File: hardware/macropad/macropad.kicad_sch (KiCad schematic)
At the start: 33 parts, among them J1 SWD, J2 USB_C_Receptacle, J4 display(4x1), J6 Enc2, J7 Enc1, SW1 SW_Push, SW11 SW_Push, SW2 SW_Push, SW3 SW_Push, SW4 SW_Push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

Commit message: added usb-c receptacle footprint
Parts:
- J2: footprint (none) -> usbc:TYPE-C-SMD_U263-163N-4GS1735
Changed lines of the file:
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@@
 			)
 		)
-		(property "Footprint" ""
+		(property "Footprint" "usbc:TYPE-C-SMD_U263-163N-4GS1735"
 			(at 361.95 170.18 0)
 			(effects

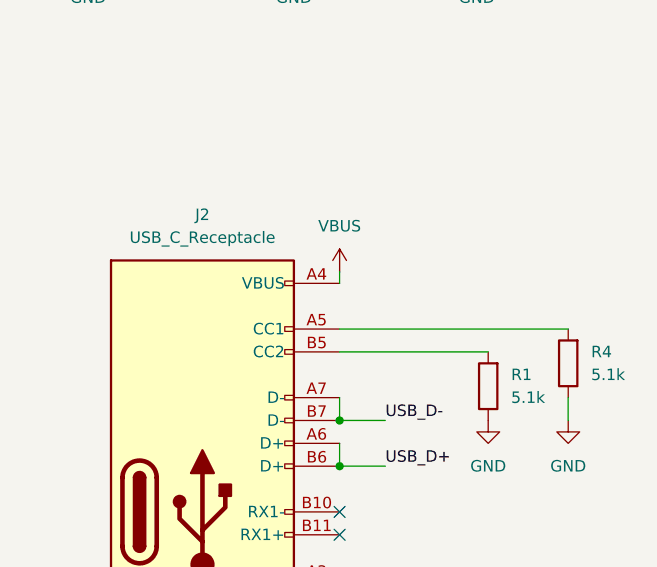
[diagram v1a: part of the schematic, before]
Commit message: erc for macropad checked
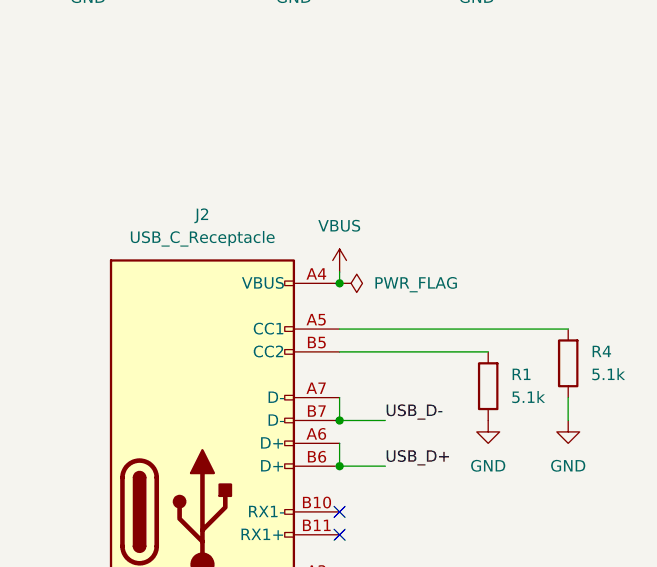
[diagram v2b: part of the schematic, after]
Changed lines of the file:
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@@
 	)
 	(junction
+		(at 373.38 144.78)
+		(diameter 0)
+		(color 0 0 0 0)
+	)
+	(junction
 		(at 288.29 53.34)
 		(diameter 0)
@@
 					(unit 1)
 				)
+			)
+		)
+	)
+	(symbol
+		(lib_id "power:PWR_FLAG")
+		(at 373.38 144.78 270)
+		(unit 1)
+		(exclude_from_sim no)
+		(in_bom yes)
+		(on_board yes)
+		(dnp no)
+		(fields_autoplaced yes)
+		(property "Reference" "#FLG01"
+			(at 375.285 144.78 0)
+			(effects
+				(font
+					(size 1.27 1.27)
+				)
+				(hide yes)
+			)
+		)
+		(property "Value" "PWR_FLAG"
+			(at 377.19 144.7799 90)
+			(effects
+				(font
+					(size 1.27 1.27)
+				)
+				(justify left)
+			)
+		)
+		(property "Footprint" ""
+			(at 373.38 144.78 0)
+			(effects
+				(font
+					(size 1.27 1.27)
+				)
+				(hide yes)
+			)
+		)
+		(property "Datasheet" "~"
+			(at 373.38 144.78 0)
+			(effects
+				(font
+					(size 1.27 1.27)
+				)
+				(hide yes)
+			)
+		)
+		(property "Description" "Special symbol for telling ERC where power comes from"
+			(at 373.38 144.78 0)
+			(effects
+				(font
+					(size 1.27 1.27)
+				)
+				(hide yes)
+			)
+		)
+		(pin "1"
+		)
+		(instances
+			(project ""
+				(path "/228dc472-b306-4e5f-8dc5-2bf23eb4978d"
+					(reference "#FLG01")
+					(unit 1)
+				)

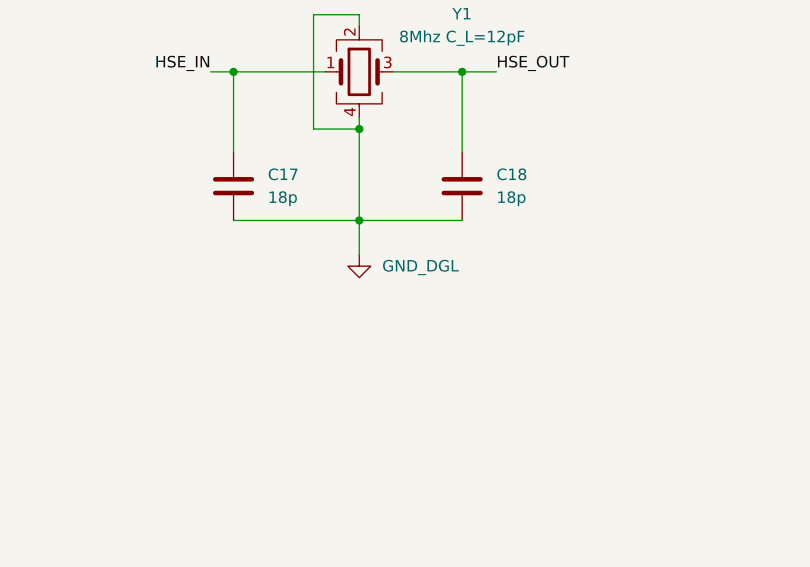
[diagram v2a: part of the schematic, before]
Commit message: added usba fp, updated pcb, 5v to vbus
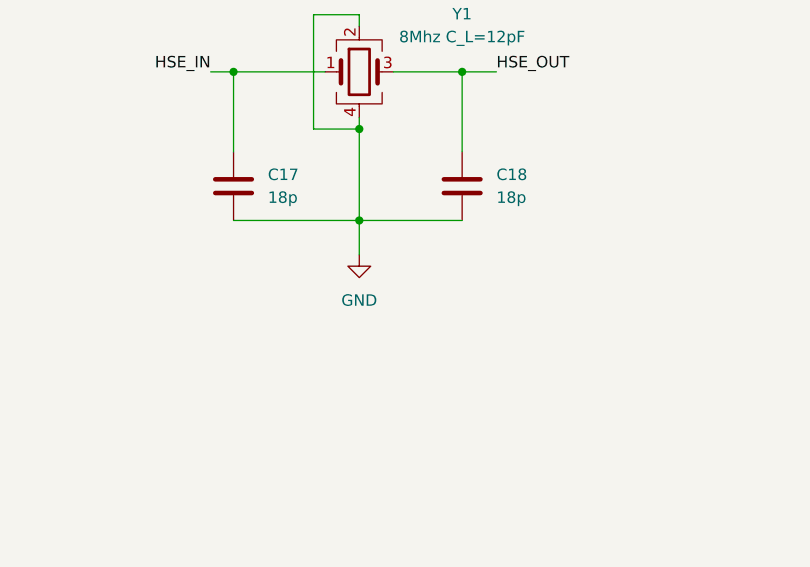
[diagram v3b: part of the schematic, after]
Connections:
- net GND_DGL is gone; now on net GND: C17.2, C18.2, Y1.2, Y1.4
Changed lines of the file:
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@@
 			)
 		)
-		(property "Value" "GND_DGL"
-			(at 104.14 147.3199 0)
+		(property "Value" "GND"
+			(at 101.6 151.13 0)
 			(effects
 				(font
 					(size 1.27 1.27)
 				)
-				(justify left)
 			)
 		)

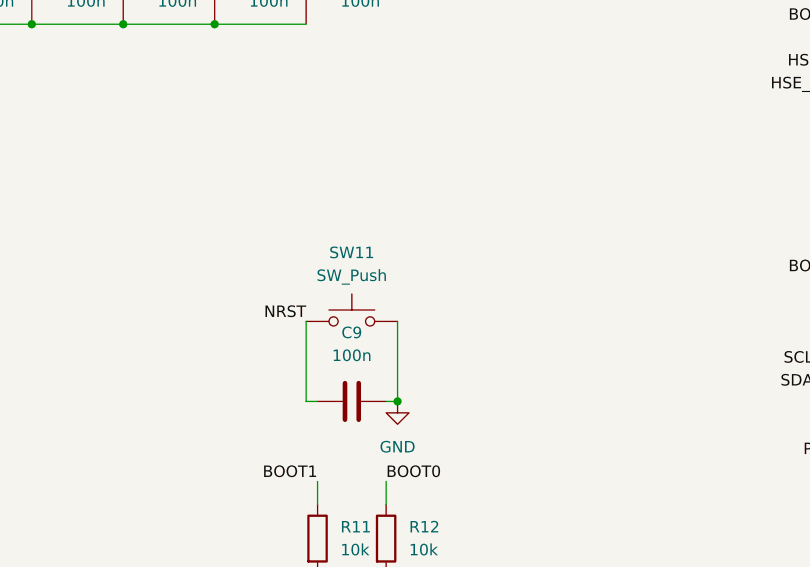
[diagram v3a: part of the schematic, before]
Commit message: replaced buttons with pads
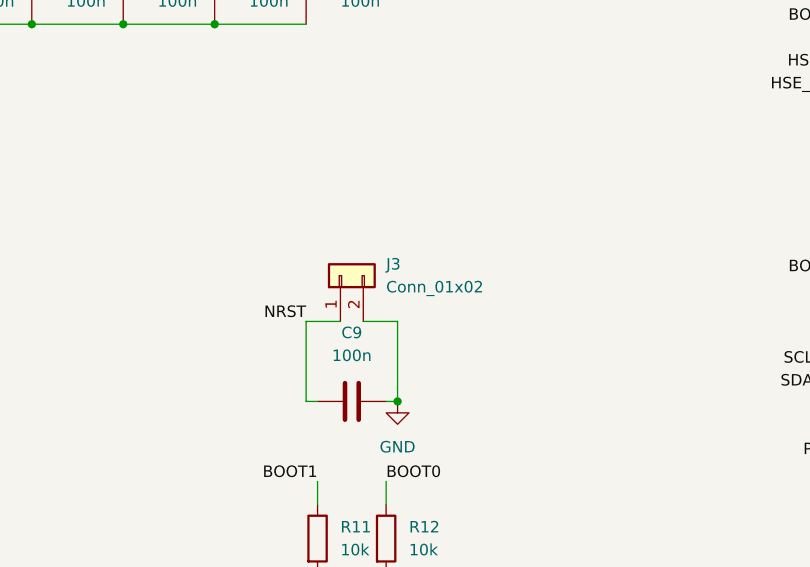
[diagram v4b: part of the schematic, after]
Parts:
- removed SW11: SW_Push, Button_Switch_SMD:SW_Push_1P1T_NO_E-Switch_TL3301NxxxxxG, symbol Switch:SW_Push
- added J3: Conn_01x02, Connector_Wire:SolderWire-0.5sqmm_1x02_P4.6mm_D0.9mm_OD2.1mm, symbol Connector_Generic:Conn_01x02
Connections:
- net GND: now also J3.2 (Pin_2)
- net NRST: now also J3.1 (Pin_1)
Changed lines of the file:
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@@
 	(wire
 		(pts
+			(xy 118.11 80.01) (xy 121.92 80.01)
+		)
+		(stroke
+			(width 0)
+			(type default)
+		)
+	)
+	(wire
+		(pts
 			(xy 96.52 119.38) (xy 96.52 132.08)
 		)
@@
 	(wire
 		(pts
+			(xy 111.76 80.01) (xy 115.57 80.01)
+		)
+		(stroke
+			(width 0)
+			(type default)
+		)
+	)
+	(wire
+		(pts
 			(xy 377.19 49.53) (xy 378.46 49.53)
 		)
@@
 	)
 	(symbol
-		(lib_id "Switch:SW_Push")
-		(at 116.84 80.01 0)
-		(unit 1)
-		(exclude_from_sim no)
-		(in_bom yes)
-		(on_board yes)
-		(dnp no)
-		(fields_autoplaced yes)
-		(property "Reference" "SW11"
-			(at 116.84 72.39 0)
-			(effects
-				(font
-					(size 1.27 1.27)
-				)
-			)
-		)
-		(property "Value" "SW_Push"
-			(at 116.84 74.93 0)
-			(effects
-				(font
-					(size 1.27 1.27)
-				)
-			)
-		)
-		(property "Footprint" "Button_Switch_SMD:SW_Push_1P1T_NO_E-Switch_TL3301NxxxxxG"
-			(at 116.84 74.93 0)
-			(effects
-				(font
-					(size 1.27 1.27)
-				)
-				(hide yes)
-			)
-		)
-		(property "Datasheet" "~"
-			(at 116.84 74.93 0)
-			(effects
-				(font
-					(size 1.27 1.27)
-				)
-				(hide yes)
-			)
-		)
-		(property "Description" "Push button switch, generic, two pins"
-			(at 116.84 80.01 0)
-			(effects
-				(font
-					(size 1.27 1.27)
-				)
-				(hide yes)
-			)
-		)
-		(pin "2"
-		)
-		(pin "1"
-		)
-		(instances
-			(project ""
-				(path "/228dc472-b306-4e5f-8dc5-2bf23eb4978d"
-					(reference "SW11")
-					(unit 1)
-				)
-			)
-		)
-	)
-	(symbol
 		(lib_id "power:GND")
 		(at 389.89 160.02 0)
@@
 					(unit 1)
 				)
+			)
+		)
+	)
+	(symbol
+		(lib_id "Connector_Generic:Conn_01x02")
+		(at 115.57 74.93 90)
+		(unit 1)
+		(exclude_from_sim no)
+		(in_bom yes)
+		(on_board yes)
+		(dnp no)
+		(fields_autoplaced yes)
+		(property "Reference" "J3"
+			(at 120.65 73.6599 90)
+			(effects
+				(font
+					(size 1.27 1.27)
+				)
+				(justify right)
+			)
+		)
+		(property "Value" "Conn_01x02"
+			(at 120.65 76.1999 90)
+			(effects
+				(font
+					(size 1.27 1.27)
+				)
+				(justify right)
+			)
+		)
+		(property "Footprint" "Connector_Wire:SolderWire-0.5sqmm_1x02_P4.6mm_D0.9mm_OD2.1mm"
+			(at 115.57 74.93 0)
+			(effects
+				(font
+					(size 1.27 1.27)
+				)
+				(hide yes)
+			)
+		)
+		(property "Datasheet" "~"
+			(at 115.57 74.93 0)
+			(effects
+				(font
+					(size 1.27 1.27)
+				)
+				(hide yes)
+			)
+		)
+		(property "Description" "Generic connector, single row, 01x02, script generated (kicad-library-utils/schlib/autogen/connector/)"
+			(at 115.57 74.93 0)
+			(effects
+				(font
+					(size 1.27 1.27)
+				)
+				(hide yes)
+			)
+		)
+		(pin "2"
+		)
+		(pin "1"
+		)
+		(instances
+			(project "macropad"
+				(path "/228dc472-b306-4e5f-8dc5-2bf23eb4978d"
+					(reference "J3")
+					(unit 1)
+				)

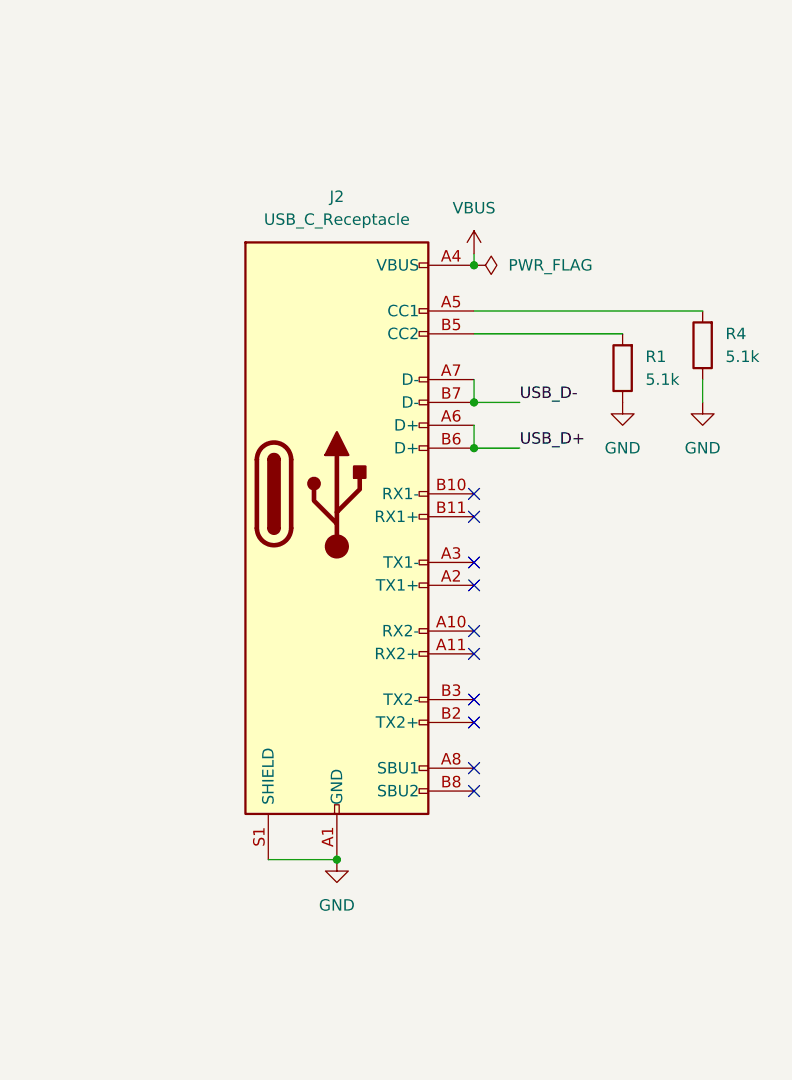
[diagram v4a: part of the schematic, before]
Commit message: updated usb-c receptacle footprint
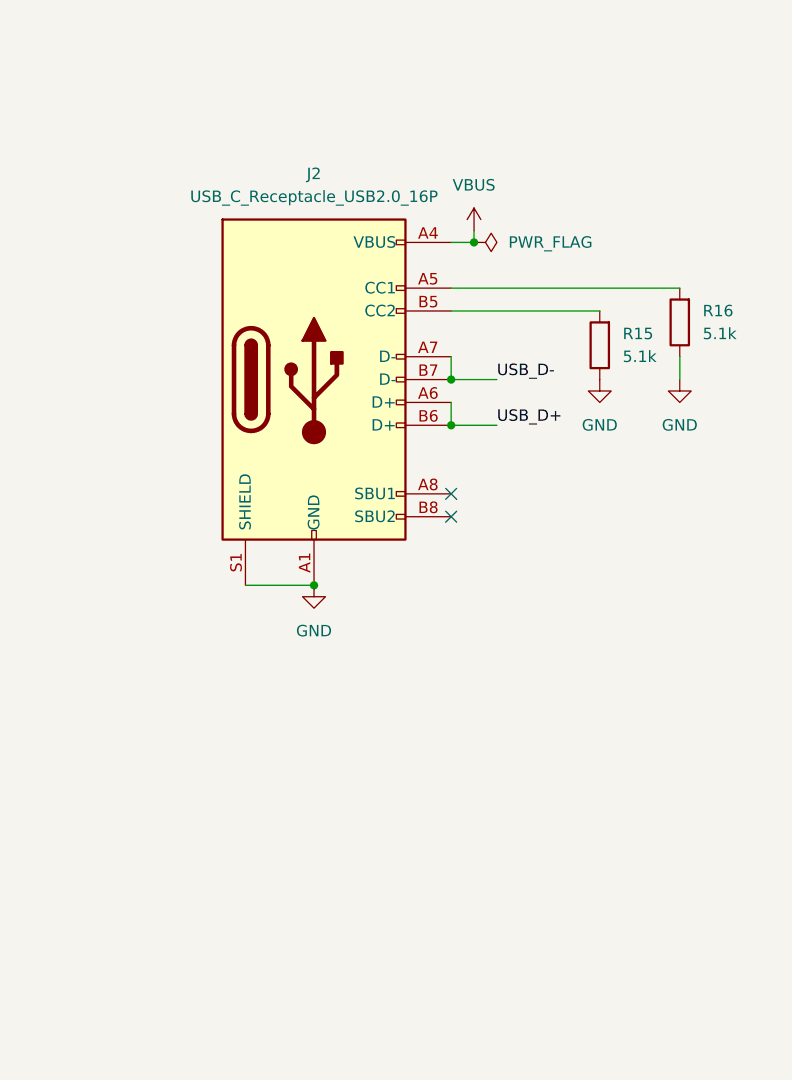
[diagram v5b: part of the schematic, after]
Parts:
- removed J2: USB_C_Receptacle, usbc:TYPE-C-SMD_U263-163N-4GS1735, symbol Connector:USB_C_Receptacle
- removed R1, R4: 5.1k, Resistor_SMD:R_0603_1608Metric, symbol Device:R
- added J2: USB_C_Receptacle_USB2.0_16P, usbc:TYPE-C-SMD_U263-163N-4GS1735, symbol Connector:USB_C_Receptacle_USB2.0_16P
- added R15, R16: 5.1k, Resistor_SMD:R_0603_1608Metric, symbol Device:R
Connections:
- net GND: now also J2.A1 (GND), J2.A12 (GND), J2.B1 (GND), J2.B12 (GND), J2.S1 (SHIELD), R15.1, R16.1
- net USB_D+: now also J2.A6 (D+), J2.B6 (D+)
- net USB_D-: now also J2.A7 (D-), J2.B7 (D-)
- net VBUS: now also J2.A4 (VBUS), J2.A9 (VBUS), J2.B4 (VBUS), J2.B9 (VBUS)
- new net: J2.A5 (CC1), R16.2
- new net: J2.B5 (CC2), R15.2
- no-connect marks 17 -> 9

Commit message: updated. comments in whatsapp
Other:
- moved on the sheet: C1, C17, C18, C2, C3, C4, C5, C6, C8, C9, J1, J3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

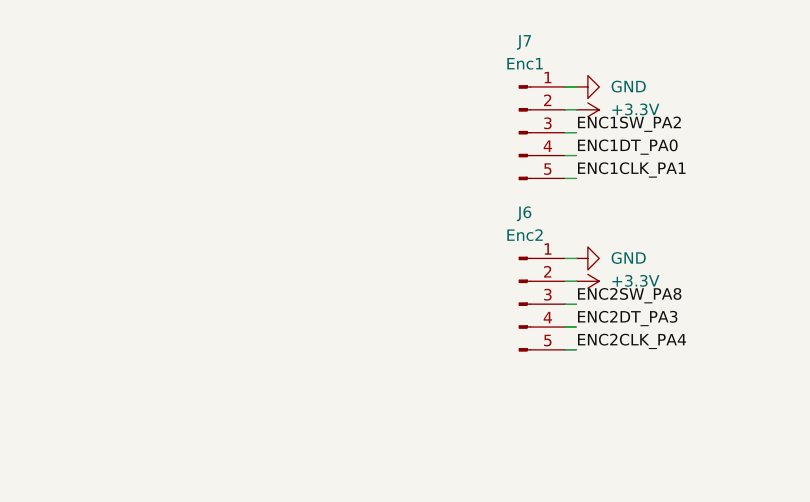
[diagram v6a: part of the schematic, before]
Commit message: pcb macropad done
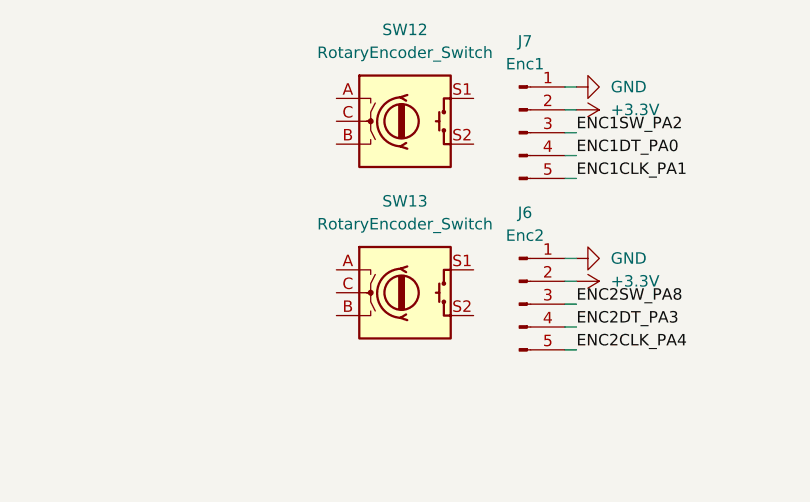
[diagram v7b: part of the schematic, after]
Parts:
- added SW12, SW13: RotaryEncoder_Switch, symbol Device:RotaryEncoder_Switch
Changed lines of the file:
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@@
+	)
+	(symbol
+		(lib_id "Device:RotaryEncoder_Switch")
+		(at 359.41 45.72 0)
+		(unit 1)
+		(exclude_from_sim no)
+		(in_bom yes)
+		(on_board yes)
+		(dnp no)
+		(fields_autoplaced yes)
+		(property "Reference" "SW13"
+			(at 359.41 35.56 0)
+			(effects
+				(font
+					(size 1.27 1.27)
+				)
+			)
+		)
+		(property "Value" "RotaryEncoder_Switch"
+			(at 359.41 38.1 0)
+			(effects
+				(font
+					(size 1.27 1.27)
+				)
+			)
+		)
+		(property "Footprint" ""
+			(at 355.6 41.656 0)
+			(effects
+				(font
+					(size 1.27 1.27)
+				)
+				(hide yes)
+			)
+		)
+		(property "Datasheet" "~"
+			(at 359.41 39.116 0)
+			(effects
+				(font
+					(size 1.27 1.27)
+				)
+				(hide yes)
+			)
+		)
+		(property "Description" "Rotary encoder, dual channel, incremental quadrate outputs, with switch"
+			(at 359.41 45.72 0)
+			(effects
+				(font
+					(size 1.27 1.27)
+				)
+				(hide yes)
+			)
+		)
+		(pin "B"
+		)
+		(pin "S1"
+		)
+		(pin "C"
+		)
+		(pin "S2"
+		)
+		(pin "A"
+		)
+		(instances
+			(project "macropad"
+				(path "/228dc472-b306-4e5f-8dc5-2bf23eb4978d"
+					(reference "SW13")
+					(unit 1)
+				)
+			)
+		)
 	)
 	(symbol
@@
 					(unit 1)
 				)
+			)
+		)
+	)
+	(symbol
+		(lib_id "Device:RotaryEncoder_Switch")
+		(at 359.41 26.67 0)
+		(unit 1)
+		(exclude_from_sim no)
+		(in_bom yes)
+		(on_board yes)
+		(dnp no)
+		(fields_autoplaced yes)
+		(property "Reference" "SW12"
+			(at 359.41 16.51 0)
+			(effects
+				(font
+					(size 1.27 1.27)
+				)
+			)
+		)
+		(property "Value" "RotaryEncoder_Switch"
+			(at 359.41 19.05 0)
+			(effects
+				(font
+					(size 1.27 1.27)
+				)
+			)
+		)
+		(property "Footprint" ""
+			(at 355.6 22.606 0)
+			(effects
+				(font
+					(size 1.27 1.27)
+				)
+				(hide yes)
+			)
+		)
+		(property "Datasheet" "~"
+			(at 359.41 20.066 0)
+			(effects
+				(font
+					(size 1.27 1.27)
+				)
+				(hide yes)
+			)
+		)
+		(property "Description" "Rotary encoder, dual channel, incremental quadrate outputs, with switch"
+			(at 359.41 26.67 0)
+			(effects
+				(font
+					(size 1.27 1.27)
+				)
+				(hide yes)
+			)
+		)
+		(pin "B"
+		)
+		(pin "S1"
+		)
+		(pin "C"
+		)
+		(pin "S2"
+		)
+		(pin "A"
+		)
+		(instances
+			(project ""
+				(path "/228dc472-b306-4e5f-8dc5-2bf23eb4978d"
+					(reference "SW12")
+					(unit 1)
+				)

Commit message: pcb done
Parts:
- removed J6: Enc2, Connector_PinHeader_2.54mm:PinHeader_1x05_P2.54mm_Vertical, symbol Connector:Conn_01x05_Pin
- removed J7: Enc1, Connector_PinHeader_2.54mm:PinHeader_1x05_P2.54mm_Vertical, symbol Connector:Conn_01x05_Pin
- added R13, R14, R17, R18, R19, R20: 10k, Resistor_SMD:R_0805_2012Metric, symbol Device:R
- SW12, SW13: footprint (none) -> Rotary_Encoder:RotaryEncoder_Alps_EC12E-Switch_Vertical_H20mm
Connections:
- net +3.3V: now also R13.2, R14.2, R17.2, R18.2, R19.2, R20.2
- net ENC1CLK_PA1: now also SW12.B, R17.1
- net ENC1DT_PA0: now also SW12.A, R14.1
- net ENC1SW_PA2: now also SW12.S1, R13.1
- net ENC2CLK_PA4: now also SW13.B, R20.1
- net ENC2DT_PA3: now also SW13.A, R19.1
- net ENC2SW_PA8: now also SW13.S1, R18.1
- net GND: now also SW12.C, SW12.S2, SW13.C, SW13.S2
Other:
- moved on the sheet: SW12, SW13
